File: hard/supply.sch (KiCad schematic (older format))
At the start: 13 parts, among them J1 MicroXNJ

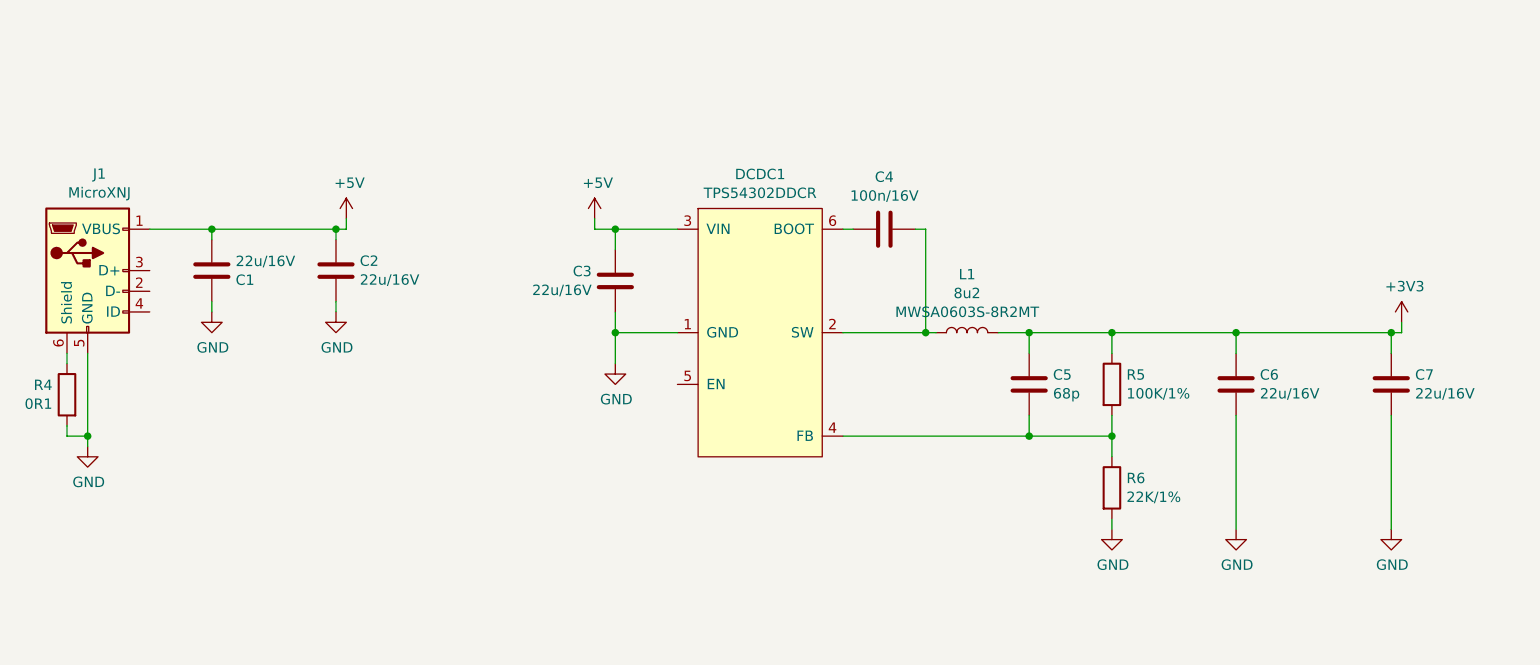
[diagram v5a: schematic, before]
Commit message: 32x32 leds on board
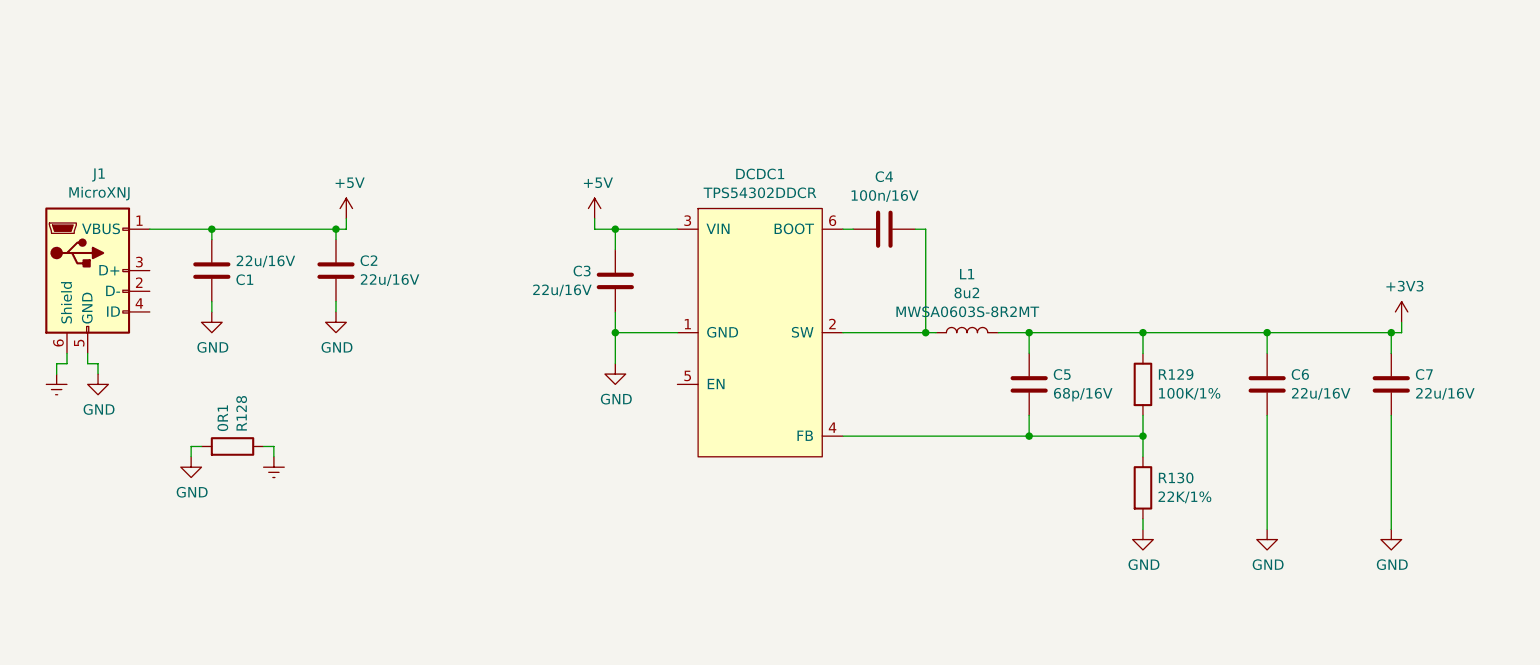
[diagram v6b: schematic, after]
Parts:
- C5: value 68p -> 68p/16V
- renumbered R4 to R128, R5 to R129, R6 to R130
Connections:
- net Earth: now reaches J1.6 (Shield), R128.1
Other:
- moved on the sheet: C6, R128, R129, R130
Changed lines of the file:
@@
 P 7300 3850
 F 0 "C5" H 7185 3804 50  0000 R CNN
-F 1 "68p" H 7185 3895 50  0000 R CNN
+F 1 "68p/16V" H 7185 3895 50  0000 R CNN
 F 2 "Capacitor_SMD:C_0402_1005Metric" H 7338 3700 50  0001 C CNN
 F 3 "~" H 7300 3850 50  0001 C CNN
@@
 $EndComp
 $Comp
-L Device:R R5
+L Device:R R129
 U 1 1 6056BF47
-P 7700 3850
-F 0 "R5" H 7770 3896 50  0000 L CNN
-F 1 "100K/1%" H 7770 3805 50  0000 L CNN
-F 2 "Resistor_SMD:R_0402_1005Metric" V 7630 3850 50  0001 C CNN
-F 3 "~" H 7700 3850 50  0001 C CNN
-	1    7700 3850
-	1    0    0    -1
-$EndComp
-$Comp
-L Device:R R6
+P 7850 3850
+F 0 "R129" H 7920 3896 50  0000 L CNN
+F 1 "100K/1%" H 7920 3805 50  0000 L CNN
+F 2 "Resistor_SMD:R_0402_1005Metric" V 7780 3850 50  0001 C CNN
+F 3 "~" H 7850 3850 50  0001 C CNN
+	1    7850 3850
+	1    0    0    -1
+$EndComp
+$Comp
+L Device:R R130
 U 1 1 6056F7CE
-P 7700 4350
-F 0 "R6" H 7770 4396 50  0000 L CNN
-F 1 "22K/1%" H 7770 4305 50  0000 L CNN
-F 2 "Resistor_SMD:R_0402_1005Metric" V 7630 4350 50  0001 C CNN
-F 3 "~" H 7700 4350 50  0001 C CNN
-	1    7700 4350
+P 7850 4350
+F 0 "R130" H 7920 4396 50  0000 L CNN
+F 1 "22K/1%" H 7920 4305 50  0000 L CNN
+F 2 "Resistor_SMD:R_0402_1005Metric" V 7780 4350 50  0001 C CNN
+F 3 "~" H 7850 4350 50  0001 C CNN
+	1    7850 4350
 	1    0    0    -1
 $EndComp
@@
 L Device:C C6
 U 1 1 60572E18
-P 8300 3850
-F 0 "C6" H 8185 3804 50  0000 R CNN
-F 1 "22u/16V" H 8185 3895 50  0000 R CNN
-F 2 "Capacitor_SMD:C_0805_2012Metric" H 8338 3700 50  0001 C CNN
-F 3 "~" H 8300 3850 50  0001 C CNN
-	1    8300 3850
+P 8450 3850
+F 0 "C6" H 8335 3804 50  0000 R CNN
+F 1 "22u/16V" H 8335 3895 50  0000 R CNN
+F 2 "Capacitor_SMD:C_0805_2012Metric" H 8488 3700 50  0001 C CNN
+F 3 "~" H 8450 3850 50  0001 C CNN
+	1    8450 3850
 	-1   0    0    1
 $EndComp
@@
 $EndComp
 $Comp
-L power:+3V3 #PWR014
+L power:+3V3 #PWR095
 U 1 1 60578BC3
 P 9100 3550
-F 0 "#PWR014" H 9100 3400 50  0001 C CNN
+F 0 "#PWR095" H 9100 3400 50  0001 C CNN
 F 1 "+3V3" H 9115 3723 50  0000 C CNN
 F 2 "" H 9100 3550 50  0001 C CNN
@@
 	6450 3100 6400 3100
 Wire Wire Line
-	7700 4200 7700 4100
-Connection ~ 7700 4100
-Wire Wire Line
-	7700 4100 7700 4000
+	7850 4200 7850 4100
+Connection ~ 7850 4100
+Wire Wire Line
+	7850 4100 7850 4000
 Wire Wire Line
 	7300 4000 7300 4100
-Connection ~ 7300 4100
-Wire Wire Line
-	7700 3700 7700 3600
-Wire Wire Line
-	7700 3600 7300 3600
+Wire Wire Line
+	7850 3700 7850 3600
 Wire Wire Line
 	7300 3700 7300 3600
-Connection ~ 7300 3600
 Wire Wire Line
 	7300 3600 7150 3600
@@
 	6800 3600 6400 3600
 $Comp
-L power:+5V #PWR09
+L power:+5V #PWR090
 U 1 1 6057B855
 P 5200 3050
-F 0 "#PWR09" H 5200 2900 50  0001 C CNN
+F 0 "#PWR090" H 5200 2900 50  0001 C CNN
 F 1 "+5V" H 5215 3223 50  0000 C CNN
 F 2 "" H 5200 3050 50  0001 C CNN
@@
 	5300 3600 5300 3500
 $Comp
-L power:GND #PWR010
+L power:GND #PWR091
 U 1 1 60575673
 P 5300 3750
-F 0 "#PWR010" H 5300 3500 50  0001 C CNN
+F 0 "#PWR091" H 5300 3500 50  0001 C CNN
 F 1 "GND" H 5305 3577 50  0000 C CNN
 F 2 "" H 5300 3750 50  0001 C CNN
@@
 Connection ~ 5300 3600
 Wire Wire Line
-	7300 4100 7700 4100
-Wire Wire Line
 	6400 4100 7300 4100
 $Comp
-L power:GND #PWR012
+L power:GND #PWR093
 U 1 1 605811D8
-P 8300 4550
-F 0 "#PWR012" H 8300 4300 50  0001 C CNN
-F 1 "GND" H 8305 4377 50  0000 C CNN
-F 2 "" H 8300 4550 50  0001 C CNN
-F 3 "" H 8300 4550 50  0001 C CNN
-	1    8300 4550
-	1    0    0    -1
-$EndComp
-Wire Wire Line
-	7700 3600 8300 3600
+P 8450 4550
+F 0 "#PWR093" H 8450 4300 50  0001 C CNN
+F 1 "GND" H 8455 4377 50  0000 C CNN
+F 2 "" H 8450 4550 50  0001 C CNN
+F 3 "" H 8450 4550 50  0001 C CNN
+	1    8450 4550
+	1    0    0    -1
+$EndComp
 Wire Wire Line
 	9050 3600 9050 3700
-Connection ~ 7700 3600
-Wire Wire Line
-	8300 3700 8300 3600
-Connection ~ 8300 3600
-Wire Wire Line
-	8300 3600 9050 3600
-$Comp
-L power:GND #PWR013
+Connection ~ 7850 3600
+Wire Wire Line
+	8450 3700 8450 3600
+Connection ~ 8450 3600
+$Comp
+L power:GND #PWR094
 U 1 1 605828FA
 P 9050 4550
-F 0 "#PWR013" H 9050 4300 50  0001 C CNN
+F 0 "#PWR094" H 9050 4300 50  0001 C CNN
 F 1 "GND" H 9055 4377 50  0000 C CNN
 F 2 "" H 9050 4550 50  0001 C CNN
@@
 $EndComp
 $Comp
-L power:GND #PWR011
+L power:GND #PWR092
 U 1 1 6057A1D3
-P 7700 4550
-F 0 "#PWR011" H 7700 4300 50  0001 C CNN
-F 1 "GND" H 7705 4377 50  0000 C CNN
-F 2 "" H 7700 4550 50  0001 C CNN
-F 3 "" H 7700 4550 50  0001 C CNN
-	1    7700 4550
+P 7850 4550
+F 0 "#PWR092" H 7850 4300 50  0001 C CNN
+F 1 "GND" H 7855 4377 50  0000 C CNN
+F 2 "" H 7850 4550 50  0001 C CNN
+F 3 "" H 7850 4550 50  0001 C CNN
+	1    7850 4550
 	1    0    0    -1
 $EndComp
@@
 Connection ~ 9050 3600
 Wire Wire Line
-	7700 4550 7700 4500
-Wire Wire Line
-	8300 4550 8300 4000
+	7850 4550 7850 4500
+Wire Wire Line
+	8450 4550 8450 4000
 Wire Wire Line
 	9050 4550 9050 4000
@@
 $EndComp
 $Comp
-L power:+5V #PWR08
+L power:+5V #PWR089
 U 1 1 6056C9AF
 P 4000 3050
-F 0 "#PWR08" H 4000 2900 50  0001 C CNN
+F 0 "#PWR089" H 4000 2900 50  0001 C CNN
 F 1 "+5V" H 4015 3223 50  0000 C CNN
 F 2 "" H 4000 3050 50  0001 C CNN
@@
 $EndComp
 $Comp
-L power:GND #PWR05
+L power:GND #PWR086
 U 1 1 6056D447
-P 2750 4150
-F 0 "#PWR05" H 2750 3900 50  0001 C CNN
-F 1 "GND" H 2755 3977 50  0000 C CNN
-F 2 "" H 2750 4150 50  0001 C CNN
-F 3 "" H 2750 4150 50  0001 C CNN
-	1    2750 4150
-	1    0    0    -1
-$EndComp
-Wire Wire Line
-	2750 4100 2750 3700
-Wire Wire Line
-	2650 4100 2750 4100
-Connection ~ 2750 4100
-Wire Wire Line
-	2750 4150 2750 4100
-Wire Wire Line
-	2650 4050 2650 4100
-Wire Wire Line
-	2650 3750 2650 3700
-$Comp
-L Device:R R4
+P 2800 3800
+F 0 "#PWR086" H 2800 3550 50  0001 C CNN
+F 1 "GND" H 2805 3627 50  0000 C CNN
+F 2 "" H 2800 3800 50  0001 C CNN
+F 3 "" H 2800 3800 50  0001 C CNN
+	1    2800 3800
+	1    0    0    -1
+$EndComp
+$Comp
+L Device:R R128
 U 1 1 6056E34B
-P 2650 3900
-F 0 "R4" H 2720 3946 50  0000 L CNN
-F 1 "0R1" H 2720 3855 50  0000 L CNN
-F 2 "Resistor_SMD:R_0805_2012Metric" V 2580 3900 50  0001 C CNN
-F 3 "~" H 2650 3900 50  0001 C CNN
-	1    2650 3900
-	-1   0    0    -1
+P 3450 4150
+F 0 "R128" H 3520 4196 50  0000 L CNN
+F 1 "0R1" H 3520 4105 50  0000 L CNN
+F 2 "Resistor_SMD:R_0805_2012Metric" V 3380 4150 50  0001 C CNN
+F 3 "~" H 3450 4150 50  0001 C CNN
+	1    3450 4150
+	0    1    -1   0
 $EndComp
 $Comp
@@
 	3350 3100 3950 3100
 $Comp
-L power:GND #PWR06
+L power:GND #PWR087
 U 1 1 6057E614
 P 3350 3500
-F 0 "#PWR06" H 3350 3250 50  0001 C CNN
+F 0 "#PWR087" H 3350 3250 50  0001 C CNN
 F 1 "GND" H 3355 3327 50  0000 C CNN
 F 2 "" H 3350 3500 50  0001 C CNN
@@
 $EndComp
 $Comp
-L power:GND #PWR07
+L power:GND #PWR088
 U 1 1 6057ED88
 P 3950 3500
-F 0 "#PWR07" H 3950 3250 50  0001 C CNN
+F 0 "#PWR088" H 3950 3250 50  0001 C CNN
 F 1 "GND" H 3955 3327 50  0000 C CNN
 F 2 "" H 3950 3500 50  0001 C CNN
@@
 Wire Wire Line
 	3950 3500 3950 3450
+$Comp
+L power:Earth #PWR?
+U 1 1 614EE00A
+P 3650 4200
+F 0 "#PWR?" H 3650 3950 50  0001 C CNN
+F 1 "Earth" H 3650 4050 50  0001 C CNN
+F 2 "" H 3650 4200 50  0001 C CNN
+F 3 "~" H 3650 4200 50  0001 C CNN
+	1    3650 4200
+	1    0    0    -1
+$EndComp
+Wire Wire Line
+	2750 3700 2750 3750
+$Comp
+L power:GND #PWR?
+U 1 1 614F0A85
+P 3250 4200
+F 0 "#PWR?" H 3250 3950 50  0001 C CNN
+F 1 "GND" H 3255 4027 50  0000 C CNN
+F 2 "" H 3250 4200 50  0001 C CNN
+F 3 "" H 3250 4200 50  0001 C CNN
+	1    3250 4200
+	1    0    0    -1
+$EndComp
+$Comp
+L power:Earth #PWR?
+U 1 1 614F2C5D
+P 2600 3800
+F 0 "#PWR?" H 2600 3550 50  0001 C CNN
+F 1 "Earth" H 2600 3650 50  0001 C CNN
+F 2 "" H 2600 3800 50  0001 C CNN
+F 3 "~" H 2600 3800 50  0001 C CNN
+	1    2600 3800
+	1    0    0    -1
+$EndComp
+Wire Wire Line
+	2650 3700 2650 3750
+Wire Wire Line
+	2650 3750 2600 3750
+Wire Wire Line
+	2600 3750 2600 3800
+Wire Wire Line
+	2750 3750 2800 3750
+Wire Wire Line
+	2800 3750 2800 3800
+Wire Wire Line
+	3250 4200 3250 4150
+Wire Wire Line
+	3250 4150 3300 4150
+Wire Wire Line
+	3600 4150 3650 4150
+Wire Wire Line
+	3650 4150 3650 4200
+Wire Wire Line
+	8450 3600 9050 3600
+Wire Wire Line
+	7850 3600 8450 3600
+Wire Wire Line
+	7300 3600 7850 3600
+Connection ~ 7300 3600
+Wire Wire Line
+	7300 4100 7850 4100
+Connection ~ 7300 4100
 $EndSCHEMATC

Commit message: led matrix schematic page completed
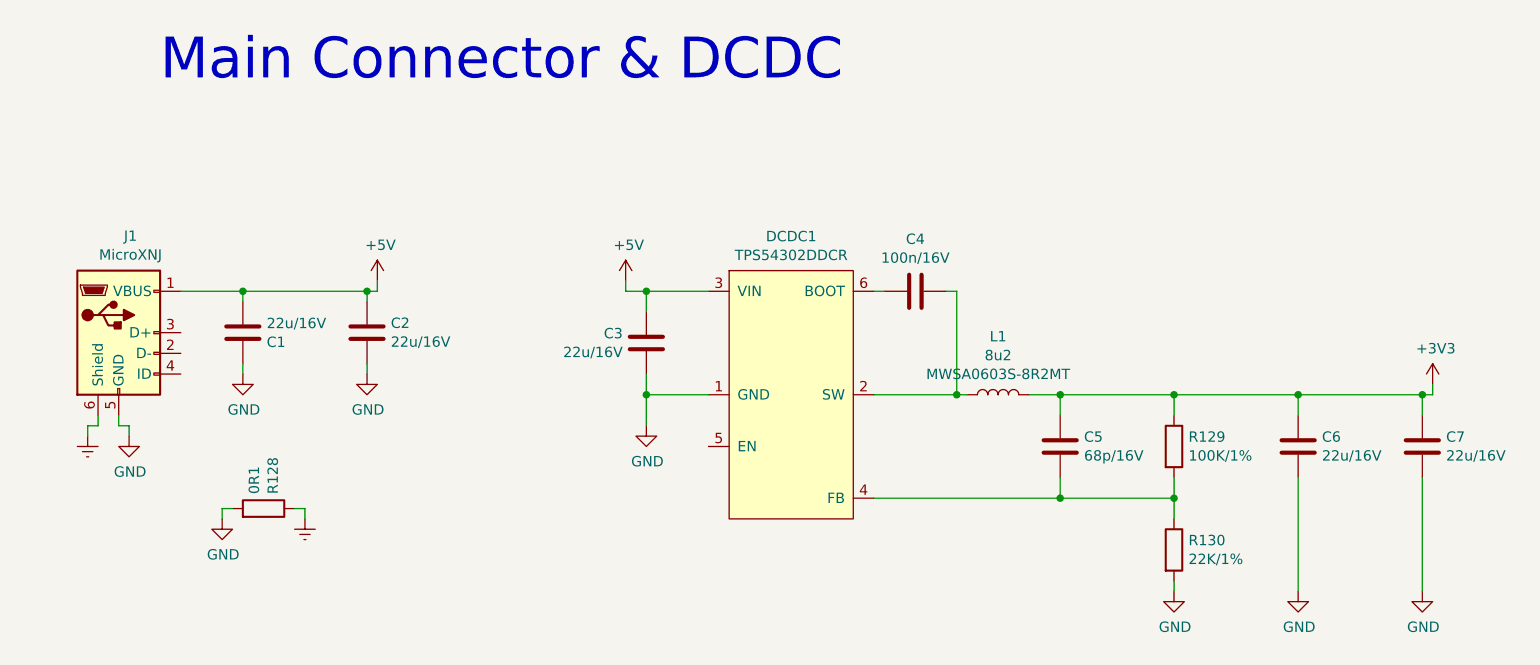
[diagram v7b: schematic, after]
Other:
- note added: "Main Connector & DCDC"
- moved on the sheet: C1, C2, C3, C4, C5, C6, C7, DCDC1, J1, L1, R128, R129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

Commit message: pc format refactor wip
@lukekaese leds still need to be attenuated
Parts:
- renumbered R128 to R193, R129 to R194, R130 to R195
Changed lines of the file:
@@
 $EndComp
 $Comp
-L Device:R R129
+L Device:R R194
 U 1 1 6056BF47
 P 8000 4150
-F 0 "R129" H 8070 4196 50  0000 L CNN
+F 0 "R194" H 8070 4196 50  0000 L CNN
 F 1 "100K/1%" H 8070 4105 50  0000 L CNN
 F 2 "Resistor_SMD:R_0402_1005Metric" V 7930 4150 50  0001 C CNN
@@
 $EndComp
 $Comp
-L Device:R R130
+L Device:R R195
 U 1 1 6056F7CE
 P 8000 4650
-F 0 "R130" H 8070 4696 50  0000 L CNN
+F 0 "R195" H 8070 4696 50  0000 L CNN
 F 1 "22K/1%" H 8070 4605 50  0000 L CNN
 F 2 "Resistor_SMD:R_0402_1005Metric" V 7930 4650 50  0001 C CNN
@@
 $EndComp
 $Comp
-L power:+3V3 #PWR095
+L power:+3V3 #PWR0173
 U 1 1 60578BC3
 P 9250 3850
-F 0 "#PWR095" H 9250 3700 50  0001 C CNN
+F 0 "#PWR0173" H 9250 3700 50  0001 C CNN
 F 1 "+3V3" H 9265 4023 50  0000 C CNN
 F 2 "" H 9250 3850 50  0001 C CNN
@@
 	6950 3900 6550 3900
 $Comp
-L power:+5V #PWR090
+L power:+5V #PWR0168
 U 1 1 6057B855
 P 5350 3350
-F 0 "#PWR090" H 5350 3200 50  0001 C CNN
+F 0 "#PWR0168" H 5350 3200 50  0001 C CNN
 F 1 "+5V" H 5365 3523 50  0000 C CNN
 F 2 "" H 5350 3350 50  0001 C CNN
@@
 	5450 3900 5450 3800
 $Comp
-L power:GND #PWR091
+L power:GND #PWR0169
 U 1 1 60575673
 P 5450 4050
-F 0 "#PWR091" H 5450 3800 50  0001 C CNN
+F 0 "#PWR0169" H 5450 3800 50  0001 C CNN
 F 1 "GND" H 5455 3877 50  0000 C CNN
 F 2 "" H 5450 4050 50  0001 C CNN
@@
 	6550 4400 7450 4400
 $Comp
-L power:GND #PWR093
+L power:GND #PWR0171
 U 1 1 605811D8
 P 8600 4850
-F 0 "#PWR093" H 8600 4600 50  0001 C CNN
+F 0 "#PWR0171" H 8600 4600 50  0001 C CNN
 F 1 "GND" H 8605 4677 50  0000 C CNN
 F 2 "" H 8600 4850 50  0001 C CNN
@@
 Connection ~ 8600 3900
 $Comp
-L power:GND #PWR094
+L power:GND #PWR0172
 U 1 1 605828FA
 P 9200 4850
-F 0 "#PWR094" H 9200 4600 50  0001 C CNN
+F 0 "#PWR0172" H 9200 4600 50  0001 C CNN
 F 1 "GND" H 9205 4677 50  0000 C CNN
 F 2 "" H 9200 4850 50  0001 C CNN
@@
 $EndComp
 $Comp
-L power:GND #PWR092
+L power:GND #PWR0170
 U 1 1 6057A1D3
 P 8000 4850
-F 0 "#PWR092" H 8000 4600 50  0001 C CNN
+F 0 "#PWR0170" H 8000 4600 50  0001 C CNN
 F 1 "GND" H 8005 4677 50  0000 C CNN
 F 2 "" H 8000 4850 50  0001 C CNN
@@
 $EndComp
 $Comp
-L power:+5V #PWR089
+L power:+5V #PWR0167
 U 1 1 6056C9AF
 P 4150 3350
-F 0 "#PWR089" H 4150 3200 50  0001 C CNN
+F 0 "#PWR0167" H 4150 3200 50  0001 C CNN
 F 1 "+5V" H 4165 3523 50  0000 C CNN
 F 2 "" H 4150 3350 50  0001 C CNN
@@
 $EndComp
 $Comp
-L power:GND #PWR086
+L power:GND #PWR0162
 U 1 1 6056D447
 P 2950 4100
-F 0 "#PWR086" H 2950 3850 50  0001 C CNN
+F 0 "#PWR0162" H 2950 3850 50  0001 C CNN
 F 1 "GND" H 2955 3927 50  0000 C CNN
 F 2 "" H 2950 4100 50  0001 C CNN
@@
 $EndComp
 $Comp
-L Device:R R128
+L Device:R R193
 U 1 1 6056E34B
 P 3600 4450
-F 0 "R128" H 3670 4496 50  0000 L CNN
+F 0 "R193" H 3670 4496 50  0000 L CNN
 F 1 "0R1" H 3670 4405 50  0000 L CNN
 F 2 "Resistor_SMD:R_0805_2012Metric" V 3530 4450 50  0001 C CNN
@@
 	3500 3400 4100 3400
 $Comp
-L power:GND #PWR087
+L power:GND #PWR0164
 U 1 1 6057E614
 P 3500 3800
-F 0 "#PWR087" H 3500 3550 50  0001 C CNN
+F 0 "#PWR0164" H 3500 3550 50  0001 C CNN
 F 1 "GND" H 3505 3627 50  0000 C CNN
 F 2 "" H 3500 3800 50  0001 C CNN
@@
 $EndComp
 $Comp
-L power:GND #PWR088
+L power:GND #PWR0166
 U 1 1 6057ED88
 P 4100 3800
-F 0 "#PWR088" H 4100 3550 50  0001 C CNN
+F 0 "#PWR0166" H 4100 3550 50  0001 C CNN
 F 1 "GND" H 4105 3627 50  0000 C CNN
 F 2 "" H 4100 3800 50  0001 C CNN
@@
 	4100 3800 4100 3750
 $Comp
-L power:Earth #PWR?
+L power:Earth #PWR0165
 U 1 1 614EE00A
 P 3800 4500
-F 0 "#PWR?" H 3800 4250 50  0001 C CNN
+F 0 "#PWR0165" H 3800 4250 50  0001 C CNN
 F 1 "Earth" H 3800 4350 50  0001 C CNN
 F 2 "" H 3800 4500 50  0001 C CNN
@@
 	2900 4000 2900 4050
 $Comp
-L power:GND #PWR?
+L power:GND #PWR0163
 U 1 1 614F0A85
 P 3400 4500
-F 0 "#PWR?" H 3400 4250 50  0001 C CNN
+F 0 "#PWR0163" H 3400 4250 50  0001 C CNN
 F 1 "GND" H 3405 4327 50  0000 C CNN
 F 2 "" H 3400 4500 50  0001 C CNN
@@
 $EndComp
 $Comp
-L power:Earth #PWR?
+L power:Earth #PWR0161
 U 1 1 614F2C5D
 P 2750 4100
-F 0 "#PWR?" H 2750 3850 50  0001 C CNN
+F 0 "#PWR0161" H 2750 3850 50  0001 C CNN
 F 1 "Earth" H 2750 3950 50  0001 C CNN
 F 2 "" H 2750 4100 50  0001 C CNN
